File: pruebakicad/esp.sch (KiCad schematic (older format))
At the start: 1 part

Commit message: pins
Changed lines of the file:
@@
 Wire Wire Line
 	5800 4550 6050 4550
-Text GLabel 6050 4150 2    50   Input ~ 0
-SCK
-Text GLabel 6050 4250 2    50   Input ~ 0
-MISO
-Text GLabel 6050 4350 2    50   Input ~ 0
-SDA
-Text GLabel 6050 4450 2    50   Input ~ 0
-RST
-Text GLabel 6050 4550 2    50   Input ~ 0
-MOSI
 $Comp
 L power:+3V3 #PWR?
@@
 Wire Wire Line
 	5800 3750 6050 3750
-Text GLabel 6050 3750 2    50   Input ~ 0
-SCL
 $Comp
 L RF_Module:ESP32-WROOM-32 U?
@@
 Wire Wire Line
 	5800 3550 6050 3550
-Text GLabel 6050 3550 2    50   Input ~ 0
+Text HLabel 6050 3550 2    50   Input ~ 0
 SDA
+Text HLabel 6050 3750 2    50   Input ~ 0
+SCL
+Text HLabel 6050 4150 2    50   Input ~ 0
+SCK
+Text HLabel 6050 4250 2    50   Input ~ 0
+MISO
+Text HLabel 6050 4350 2    50   Input ~ 0
+SDA
+Text HLabel 6050 4450 2    50   Input ~ 0
+RST
+Text HLabel 6050 4550 2    50   Input ~ 0
+MOSI
 $EndSCHEMATC

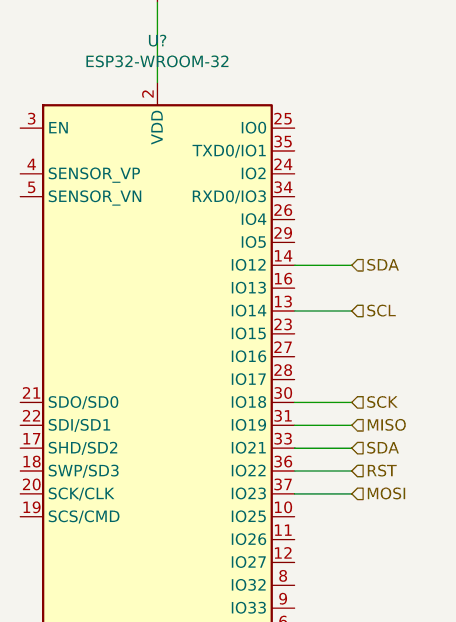
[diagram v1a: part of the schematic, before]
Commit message: More peripherals
Added some peripherals and last ones were fixed
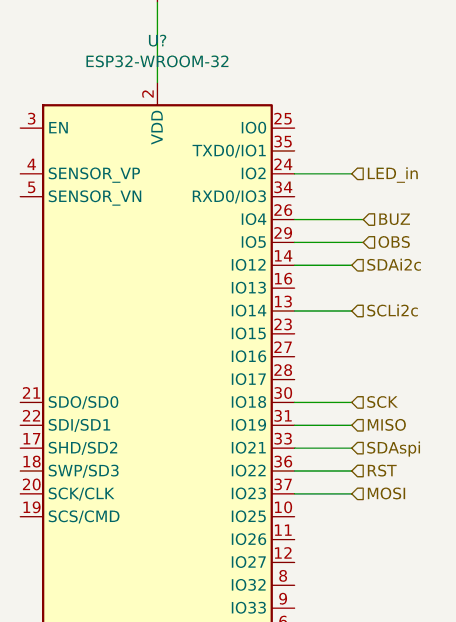
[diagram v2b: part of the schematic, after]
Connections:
- net LED_in: now reaches U?.24 (IO2)
- net BUZ: now reaches U?.26 (IO4)
- net OBS: now reaches U?.29 (IO5)
- net SCL renamed SCLi2c
- net SDA renamed SDAi2c
- net SDAi2c: no longer U?.33 (IO21)
- new net SDAspi: U?.33 (IO21)
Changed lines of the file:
@@
 	5800 3550 6050 3550
 Text HLabel 6050 3550 2    50   Input ~ 0
-SDA
+SDAi2c
 Text HLabel 6050 3750 2    50   Input ~ 0
-SCL
+SCLi2c
 Text HLabel 6050 4150 2    50   Input ~ 0
 SCK
@@
 MISO
 Text HLabel 6050 4350 2    50   Input ~ 0
-SDA
+SDAspi
 Text HLabel 6050 4450 2    50   Input ~ 0
 RST
 Text HLabel 6050 4550 2    50   Input ~ 0
 MOSI
+Wire Wire Line
+	5800 3150 6050 3150
+Text HLabel 6050 3150 2    50   Input ~ 0
+LED_in
+Wire Wire Line
+	5800 3350 6100 3350
+Text HLabel 6100 3350 2    50   Input ~ 0
+BUZ
+Wire Wire Line
+	5800 3450 6100 3450
+Text HLabel 6100 3450 2    50   Input ~ 0
+OBS
 $EndSCHEMATC

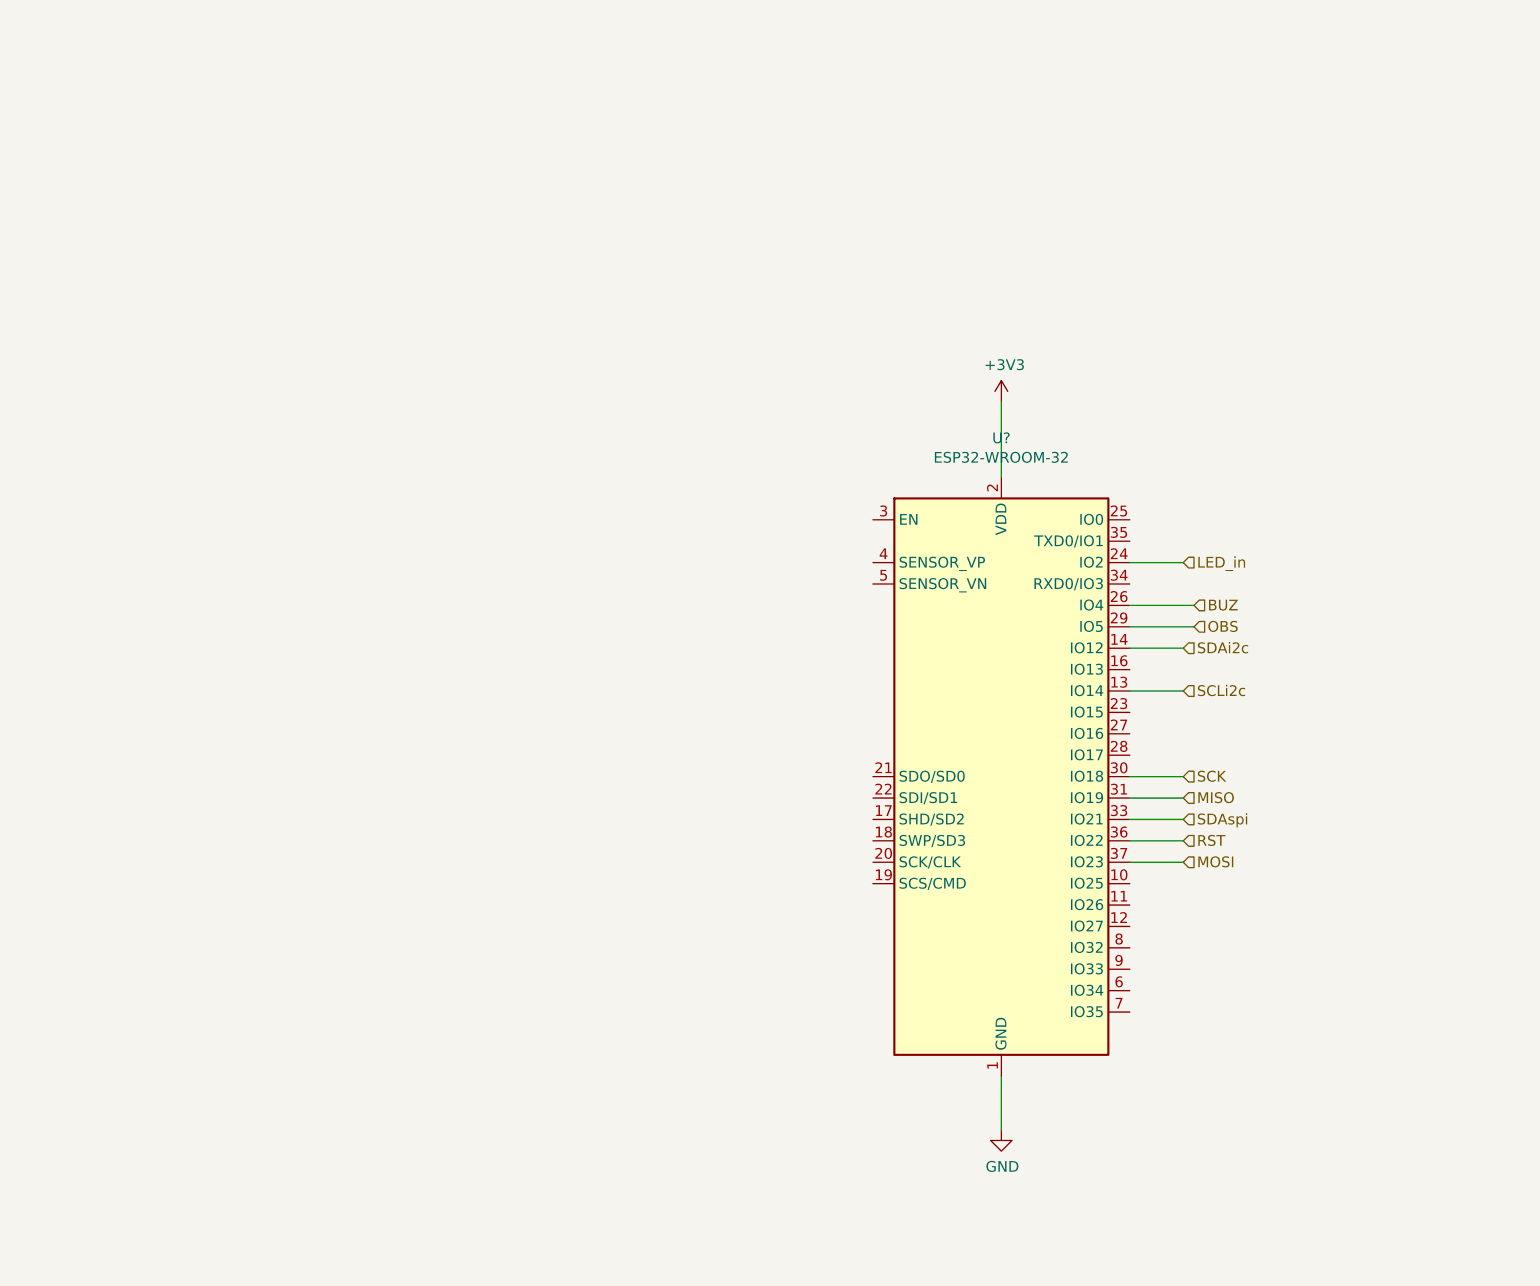
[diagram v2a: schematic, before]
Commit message: Added_gpios
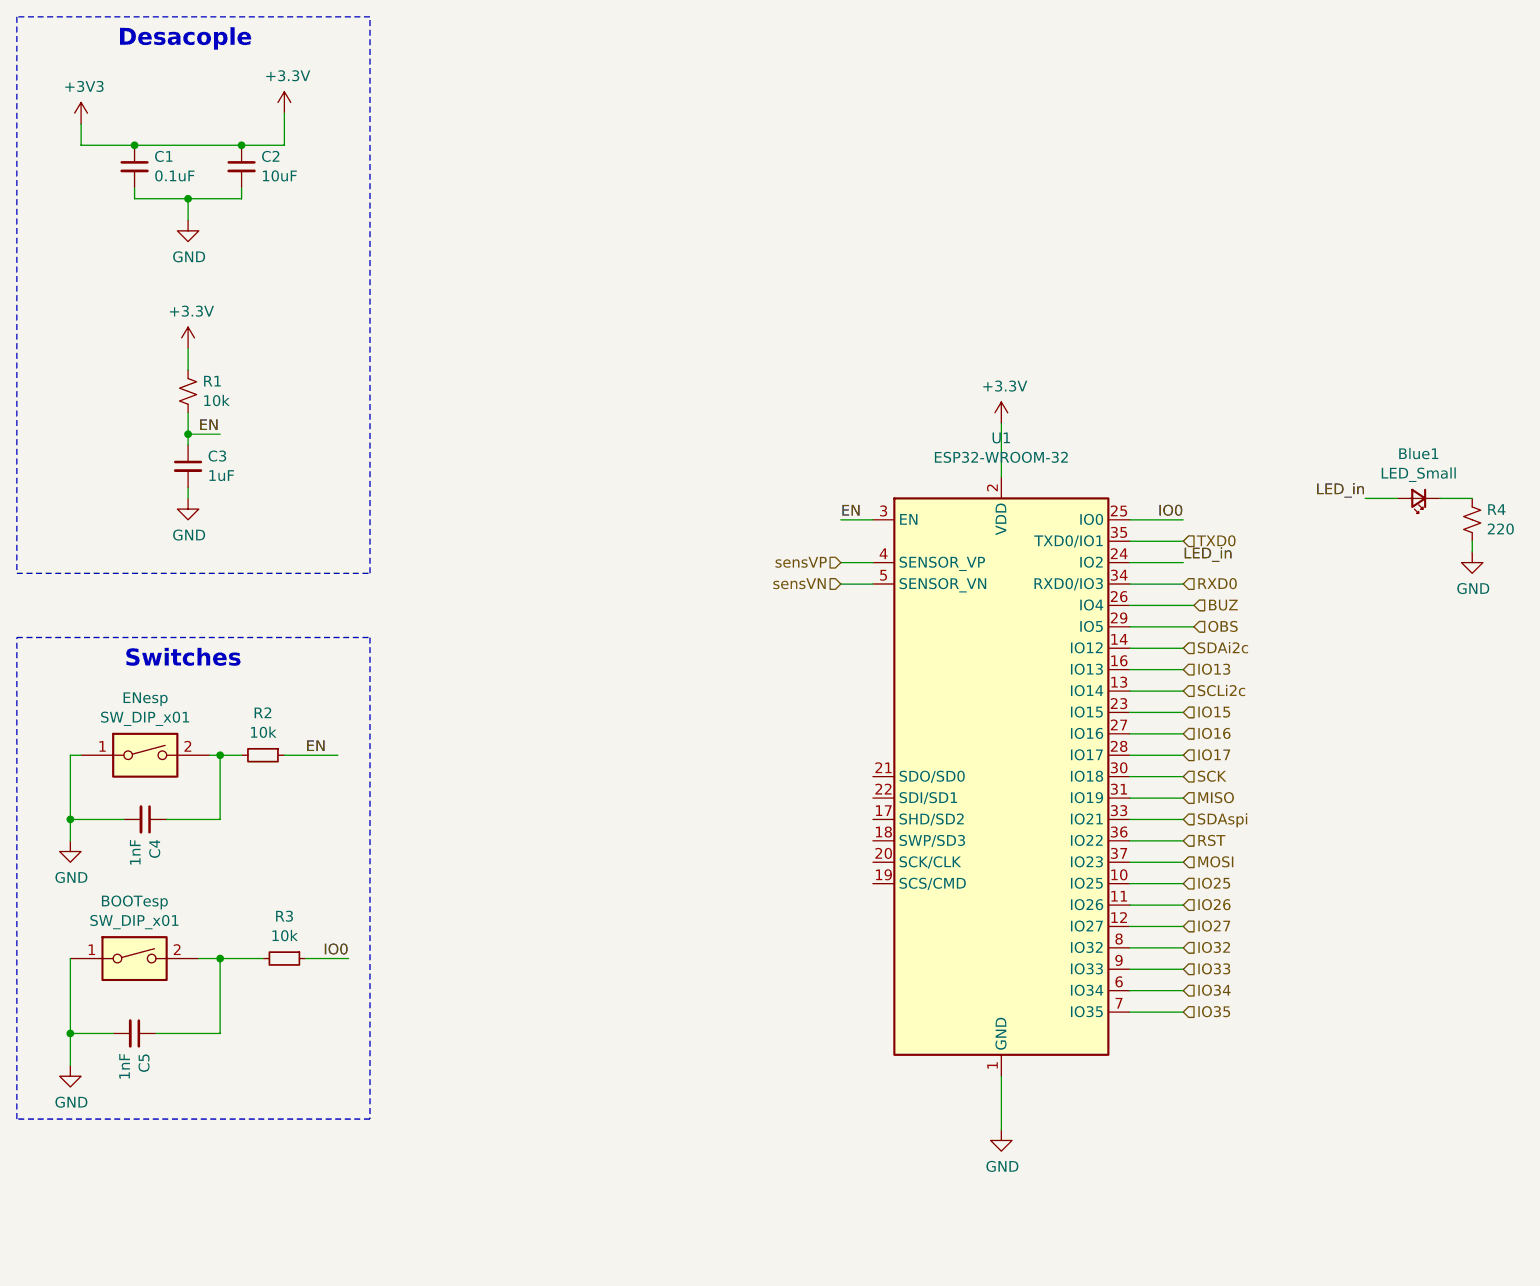
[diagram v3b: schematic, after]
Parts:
- added BOOTesp, ENesp: SW_DIP_x01, symbol Switch:SW_DIP_x01
- added Blue1: LED_Small, symbol Device:LED_Small
- added C1: 0.1uF, symbol Device:C_Small
- added C2: 10uF, symbol Device:C_Small
- added C3: 1uF, symbol Device:C_Small
- added C4, C5: 1nF, symbol Device:C_Small
- added R1: 10k, symbol Device:R_Small_US
- added R2, R3: 10k, symbol Device:R_Small
- added R4: 220, symbol Device:R_Small_US
- gave numbers to parts that had none: 1
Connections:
- net +3V3: now also C1.1, C2.1, R1.2
- net GND: now also BOOTesp.1, C1.2, C2.2, C3.2, C4.2, C5.2, ENesp.1, R4.1
- net LED_in: now also Blue1.2 (A)
- net IO25: now reaches U1.10 (IO25)
- net IO26: now reaches U1.11 (IO26)
- net IO27: now reaches U1.12 (IO27)
- net IO13: now reaches U1.16 (IO13)
- net IO15: now reaches U1.23 (IO15)
- net IO0: now reaches U1.25 (IO0)
- net IO0: now also R3.1
- net IO16: now reaches U1.27 (IO16)
- net IO17: now reaches U1.28 (IO17)
- net EN: now reaches U1.3 (EN)
- net EN: now also C3.1, R1.1, R2.1
- net RXD0: now reaches U1.34 (RXD0/IO3)
- net TXD0: now reaches U1.35 (TXD0/IO1)
- net sensVP: now reaches U1.4 (SENSOR_VP)
- net sensVN: now reaches U1.5 (SENSOR_VN)
- net IO34: now reaches U1.6 (IO34)
- net IO35: now reaches U1.7 (IO35)
- net IO32: now reaches U1.8 (IO32)
- net IO33: now reaches U1.9 (IO33)
- new net: Blue1.1 (K), R4.2
- new net: C4.1, ENesp.2, R2.2
- new net: BOOTesp.2, C5.1, R3.2
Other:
- note added: "Desacople"
- note added: "Switches"

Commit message: uart_added
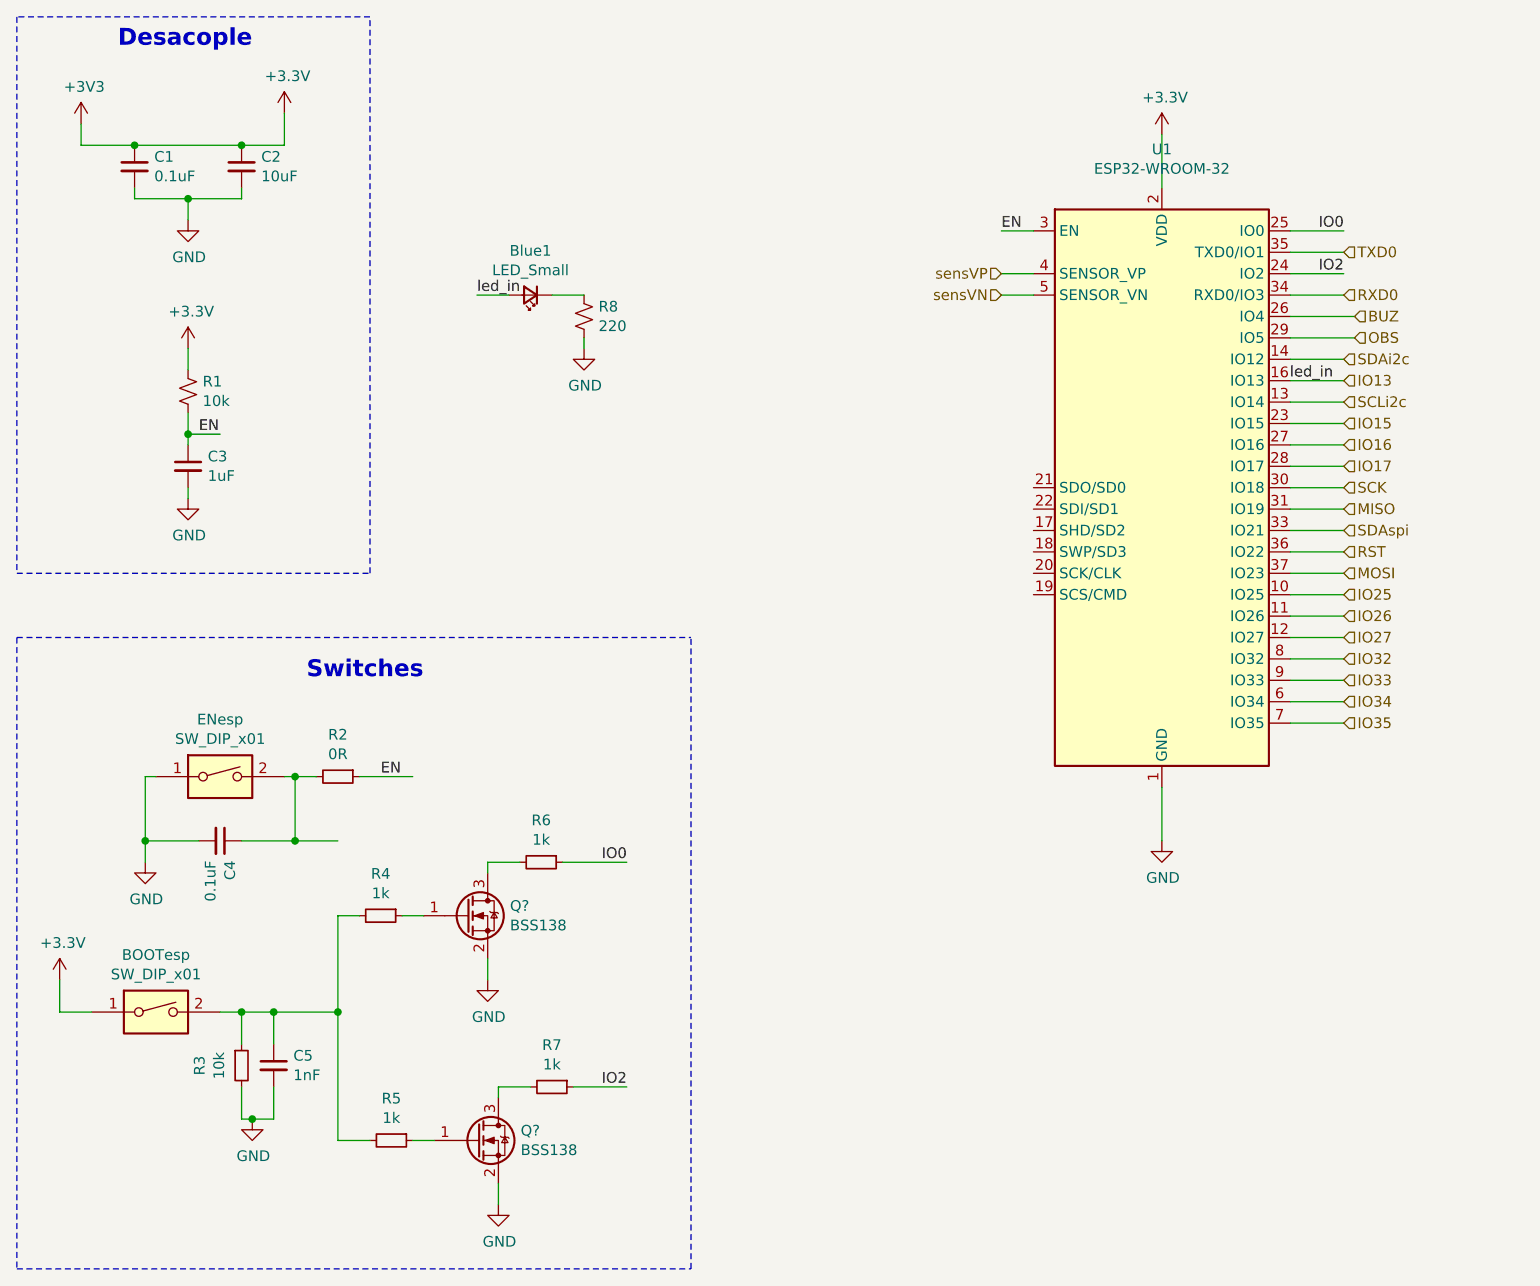
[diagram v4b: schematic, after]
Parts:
- added Q? (x2): BSS138, Package_TO_SOT_SMD:SOT-23, symbol Transistor_FET:BSS138
- added R3: 10k, symbol Device:R_Small
- added R4, R6, R7: 1k, symbol Device:R_Small
- C4: value 1nF -> 0.1uF
- R2: value 10k -> 0R
- R5: renamed from R3; value 10k -> 1k
- renumbered R4 to R8
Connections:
- net labels added: IO2, led_in
- net labels removed: LED_in
- wire segments 64 -> 82
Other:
- moved on the sheet: BOOTesp, Blue1, C4, C5, ENesp, R2, R5, R8, U1
